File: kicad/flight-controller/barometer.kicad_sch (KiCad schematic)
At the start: 5 parts

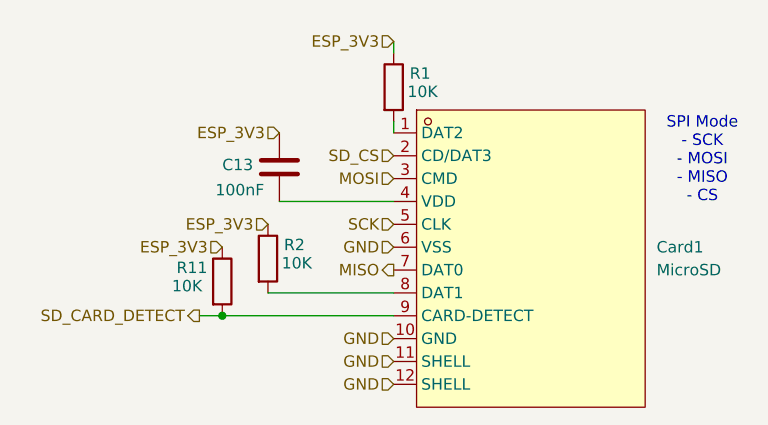
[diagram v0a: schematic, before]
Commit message: Fix ESP32 LDO thermal margin, add USB-C/SBUS ESD protection
Design review flagged the ESP32-S3's 3.3V LDO (AP2112K-3.3, SOT-23-5)
at only 1.5C margin to absolute max under WiFi load. Swapped to a
Torex XC6220B331PR-G (SOT-89-5, thermal tab tied to GND) with matching
input/output caps and thermal vias under the tab; thermal score is now
100/100 with no findings. Sensor LDO (U6) was unaffected and left as-is.

Also added TVS protection that was missing on two exposed signal paths:
D4 + bulk cap on USB-C VBUS (J13, now populated for field use) ahead of
the existing blocking diode, and a matching TVS (D6) on the RC receiver
SBUS line (J7), reusing the same part to minimize BOM diversity.

Every part number touched this pass (U4, C17-C19, D4, D6) was verified
against real distributor data, and a full BOM audit confirmed all other
assigned part numbers match their stated value and footprint. Also
removed two orphaned, unwired schematic files (airspeed.kicad_sch,
lidar.kicad_sch) that weren't in the sheet hierarchy.

Known follow-up before fab: the production/ fab package predates this
rework and needs to be regenerated, and Update PCB from Schematic needs
a re-run to sync D4/D6's display value (nets are already correct).

Co-Authored-By: Claude Sonnet 5 <noreply@anthropic.com>
Claude-Session: https://claude.ai/code/session_01NksRnW4jXLWsYwZNR7u39H
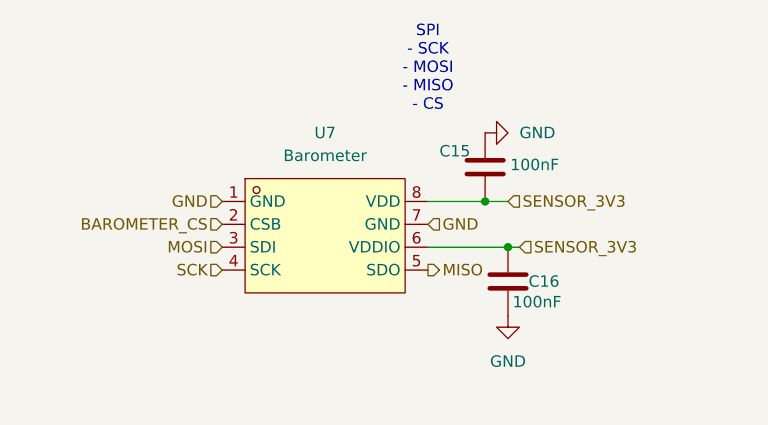
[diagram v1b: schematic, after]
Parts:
- removed C13: 100nF, Capacitor_SMD:C_0402_1005Metric, symbol Device:C
- removed Card1: MicroSD, easyeda2kicad:TF-SMD_XKTF-001B, symbol easyeda2kicad:XKTF-001B
- removed R1, R11, R2: 10K, Resistor_SMD:R_0402_1005Metric, symbol Device:R
- added C15, C16: 100nF, Capacitor_SMD:C_0402_1005Metric, symbol Device:C
- added U7: Barometer, easyeda2kicad:LGA-8_L2.5-W2.0-P0.65-TR_DPS368, symbol easyeda2kicad:DPS368XTSA1
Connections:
- net GND: now also C15.1, C16.2, U7.1 (GND), U7.7 (GND)
- net MISO: now also U7.5 (SDO)
- net MOSI: now also U7.3 (SDI)
- net SCK: now also U7.4 (SCK)
- new net BAROMETER_CS: U7.2 (CSB)
- new net SENSOR_3V3: C15.2, C16.1, U7.6 (VDDIO), U7.8 (VDD)
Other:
- note added: "SPI - SCK - MOSI - MISO - CS"
- note removed: "SPI Mode - SCK - MOSI - MISO - CS"
- title: Micro SD Card -> Barometer
